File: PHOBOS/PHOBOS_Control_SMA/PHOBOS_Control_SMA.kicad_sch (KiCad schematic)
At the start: 85 parts, among them IC10 PD2328J5050S2HF, IC4 MAPS-010144-TR0500, IC5 MAPS-010144-TR0500, IC6 MAPS-010144-TR0500, IC7 MAPS-010144-TR0500, IC8 PD2328J5050S2HF, IC9 PD2328J5050S2HF, J1 ANT3, J2 ANT4, J3 USB4056-03-A_REVA2, J4 BATT, J5 ANT1, J6 ANT2, J8 BOOT, U1 SX1280IMLTRT, U2 W25Q128JVSIQ, U3 NCP1117-3.3_SOT223, U4 RP2040, U5 TPS60403DBV, Y1 C1E-52.000-10-1012-X-M, Y2 ABM8-272-T3

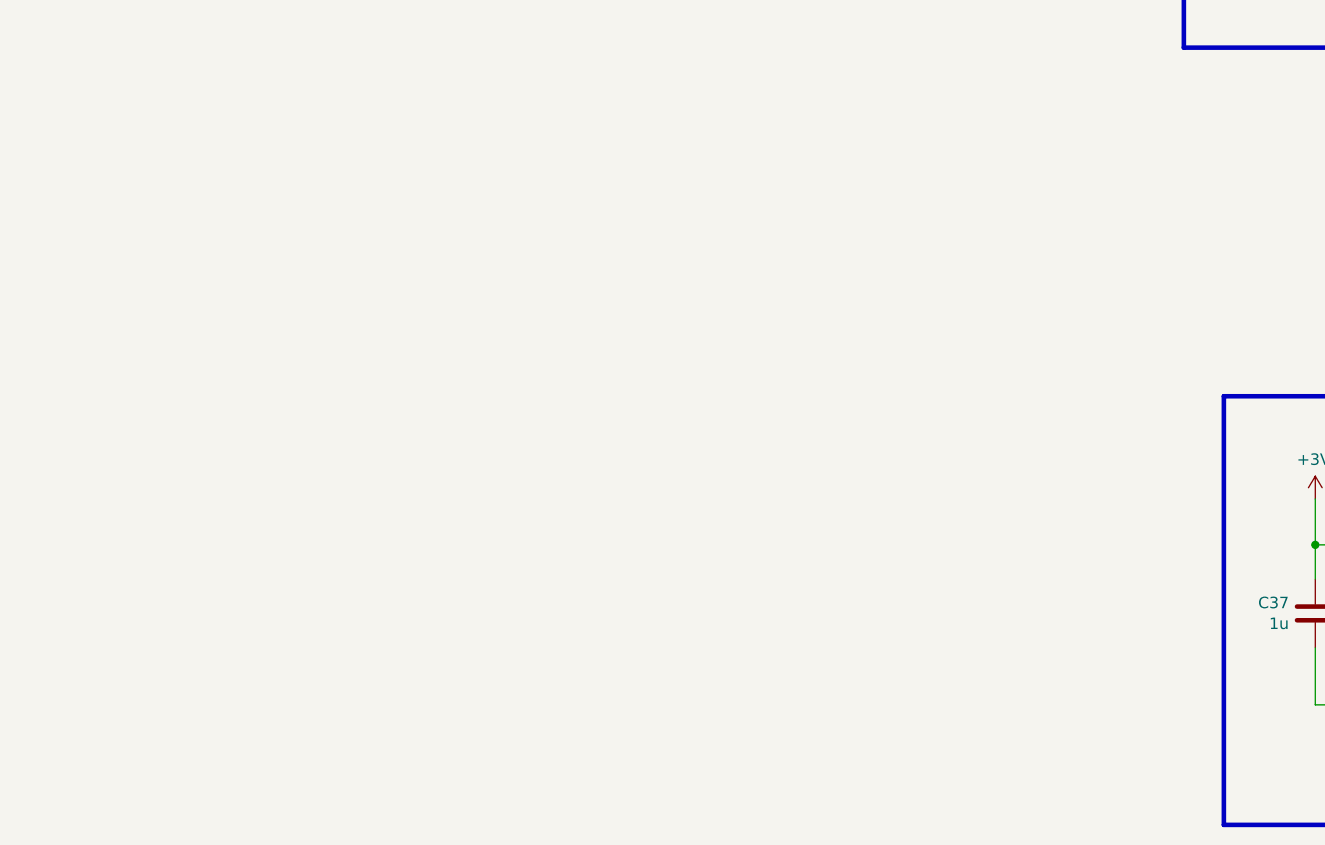
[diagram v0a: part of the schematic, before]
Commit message: sensors added to schematic and board. unlayed
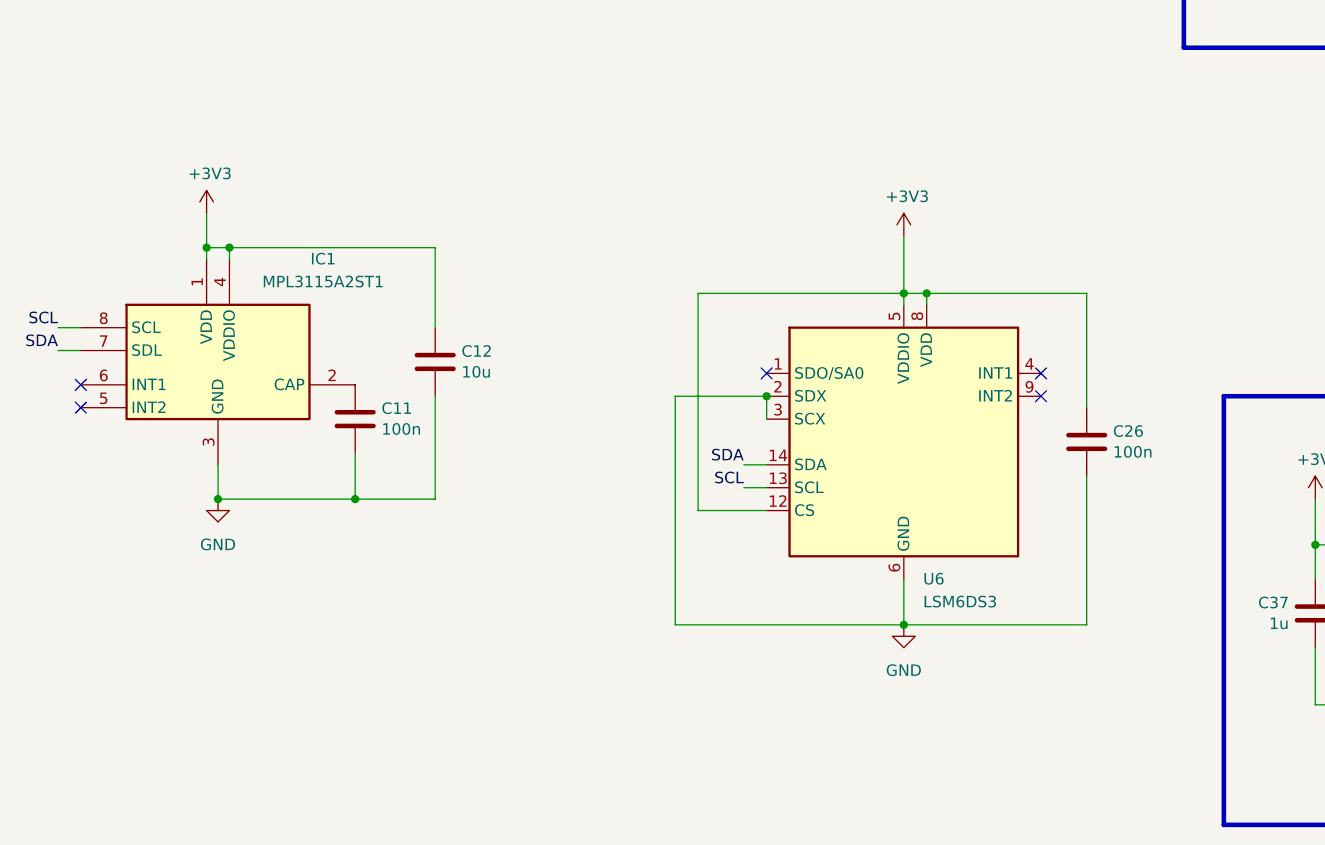
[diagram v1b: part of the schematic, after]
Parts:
- added C11, C26: 100n, Capacitor_SMD:C_0402_1005Metric, symbol Device:C
- added C12: 10u, Capacitor_SMD:C_0603_1608Metric_Pad1.08x0.95mm_HandSolder, symbol Device:C
- added IC1: MPL3115A2ST1, MPL3115A2ST1, symbol MPL3115A2ST1:MPL3115A2ST1
- added U6: LSM6DS3, Package_LGA:LGA-14_3x2.5mm_P0.5mm_LayoutBorder3x4y, symbol Sensor_Motion:LSM6DS3
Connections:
- net +3V3: now also C12.1, C26.1, IC1.1 (VDD), IC1.4 (VDDIO), U6.12 (CS), U6.5 (VDDIO), U6.8 (VDD)
- net GND: now also C11.2, C12.2, C26.2, IC1.3 (GND), U6.2 (SDX), U6.3 (SCX), U6.6 (GND), U6.7 (GND)
- net SCL: now also IC1.8 (SCL), U6.13 (SCL)
- net SDA: now also IC1.7 (SDL), U6.14 (SDA)
- new net: C11.1, IC1.2 (CAP)
- no-connect marks 36 -> 41
